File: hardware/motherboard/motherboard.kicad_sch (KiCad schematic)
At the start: 1 part

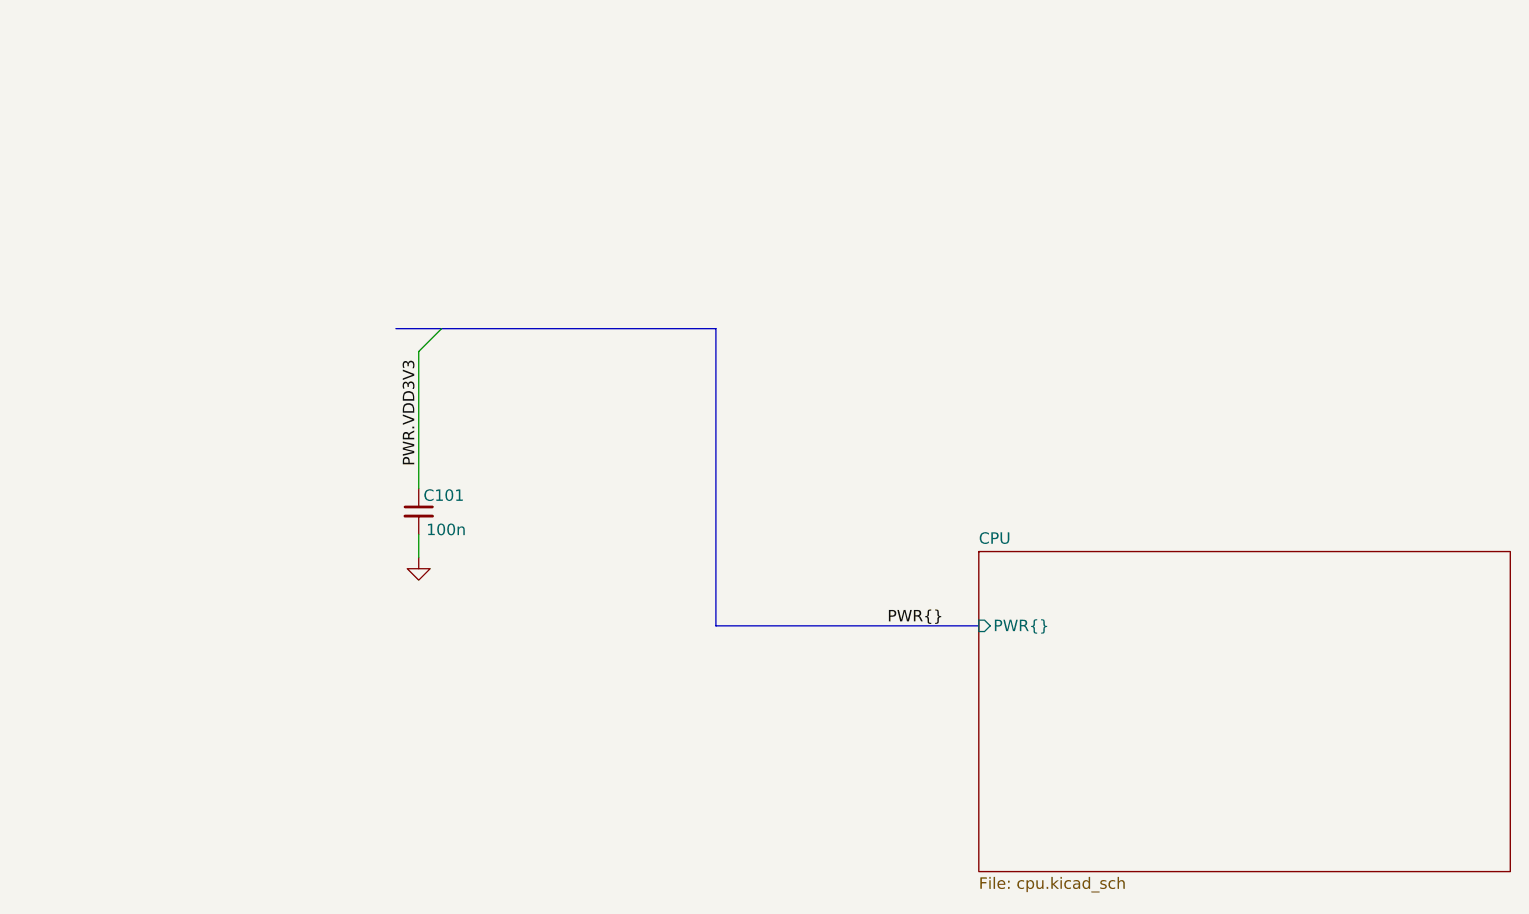
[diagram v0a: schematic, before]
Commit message: Add mp157 family datasheets, fix bus errors in schematic
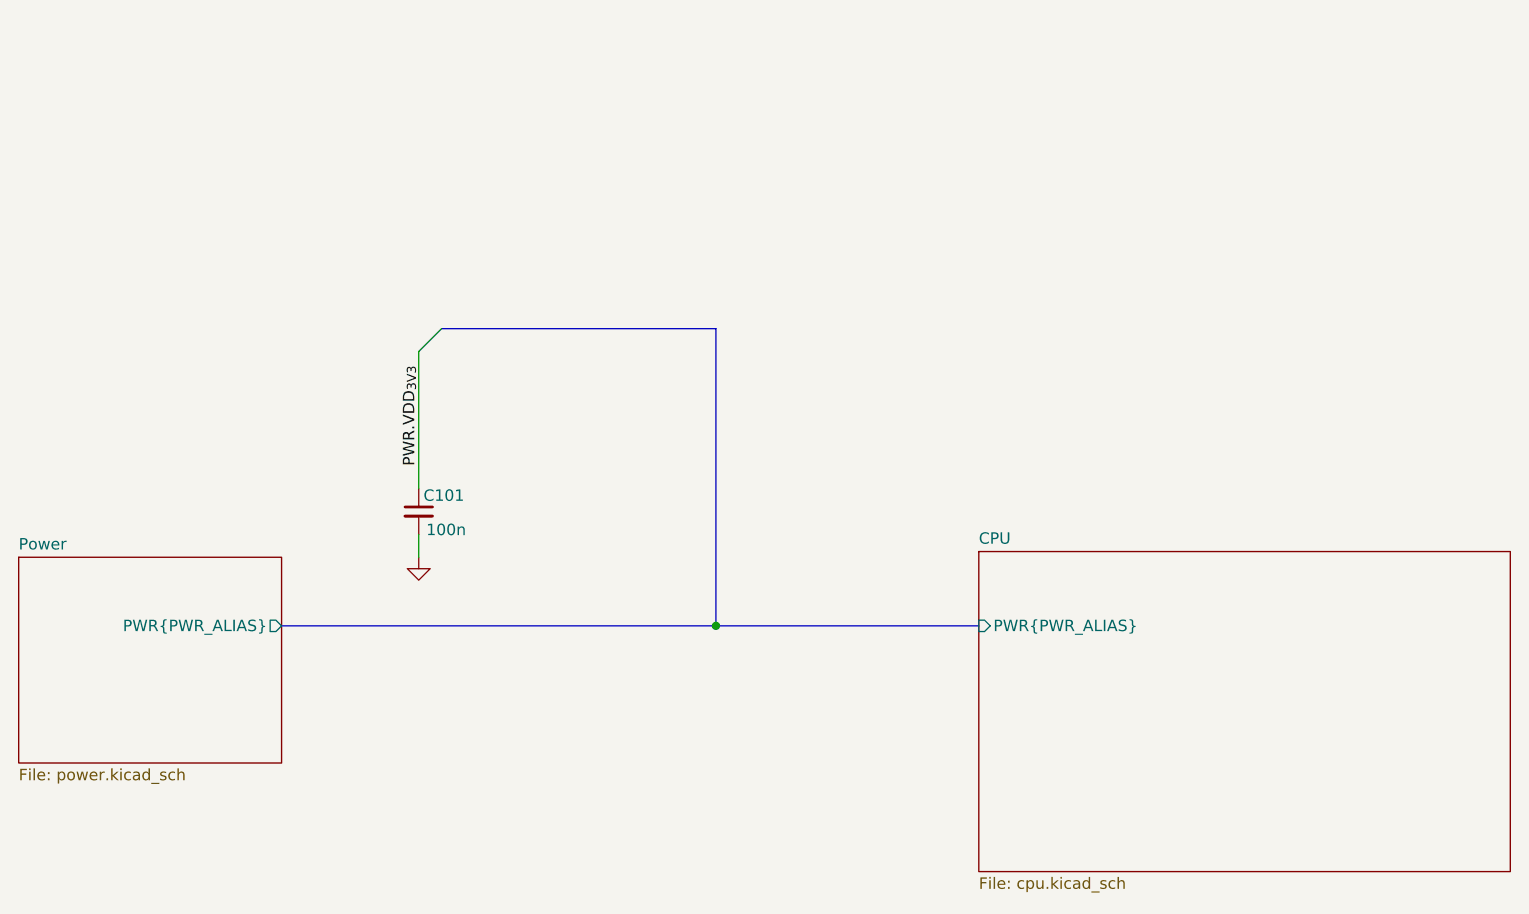
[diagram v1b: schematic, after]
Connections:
- net PWR.VDD3V3 renamed PWR.VDD_{3V3}
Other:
- added sheet Power (power.kicad_sch)
- sheet CPU ports: added PWR{PWR_ALIAS}; removed PWR{}
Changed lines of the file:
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@@
 	(generator_version "8.0")
 	(paper "A3")
+	(junction
+		(at 163.83 208.28)
+		(diameter 0)
+		(color 0 0 0 0)
+	)
 	(bus_entry
 		(at 130.81 177.8)
@@
 	(bus
 		(pts
-			(xy 128.27 175.26) (xy 133.35 175.26)
+			(xy 115.57 208.28) (xy 163.83 208.28)
 		)
 		(stroke
@@
 		)
 	)
-	(label "PWR{}"
-		(at 182.88 208.28 0)
-		(fields_autoplaced yes)
-		(effects
-			(font
-				(size 1.27 1.27)
-			)
-			(justify left bottom)
-		)
-	)
-	(label "PWR.VDD3V3"
+	(label "PWR.VDD_{3V3}"
 		(at 130.81 190.5 90)
 		(fields_autoplaced yes)
@@
 	)
 	(sheet
+		(at 86.36 200.66)
+		(size 29.21 22.86)
+		(fields_autoplaced yes)
+		(stroke
+			(width 0.1524)
+			(type solid)
+		)
+		(fill
+			(color 0 0 0 0.0000)
+		)
+		(property "Sheetname" "Power"
+			(at 86.36 199.9484 0)
+			(effects
+				(font
+					(size 1.27 1.27)
+				)
+				(justify left bottom)
+			)
+		)
+		(property "Sheetfile" "power.kicad_sch"
+			(at 86.36 224.1046 0)
+			(effects
+				(font
+					(size 1.27 1.27)
+				)
+				(justify left top)
+			)
+		)
+		(pin "PWR{PWR_ALIAS}" output
+			(at 115.57 208.28 0)
+			(effects
+				(font
+					(size 1.27 1.27)
+				)
+				(justify right)
+			)
+		)
+		(instances
+			(project "motherboard"
+				(path "/5ade21d8-1dcf-4e66-8082-2cad393a5fdd"
+					(page "3")
+				)
+			)
+		)
+	)
+	(sheet
 		(at 193.04 200.025)
 		(size 59.055 35.56)
@@
 			)
 		)
-		(pin "PWR{}" input
+		(pin "PWR{PWR_ALIAS}" input
 			(at 193.04 208.28 180)
 			(effects
@@
 		)
 		(instances
-			(project "sipzdometr"
+			(project "motherboard"
 				(path "/5ade21d8-1dcf-4e66-8082-2cad393a5fdd"
 					(page "2")

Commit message: Add RAM, models, connect RAM
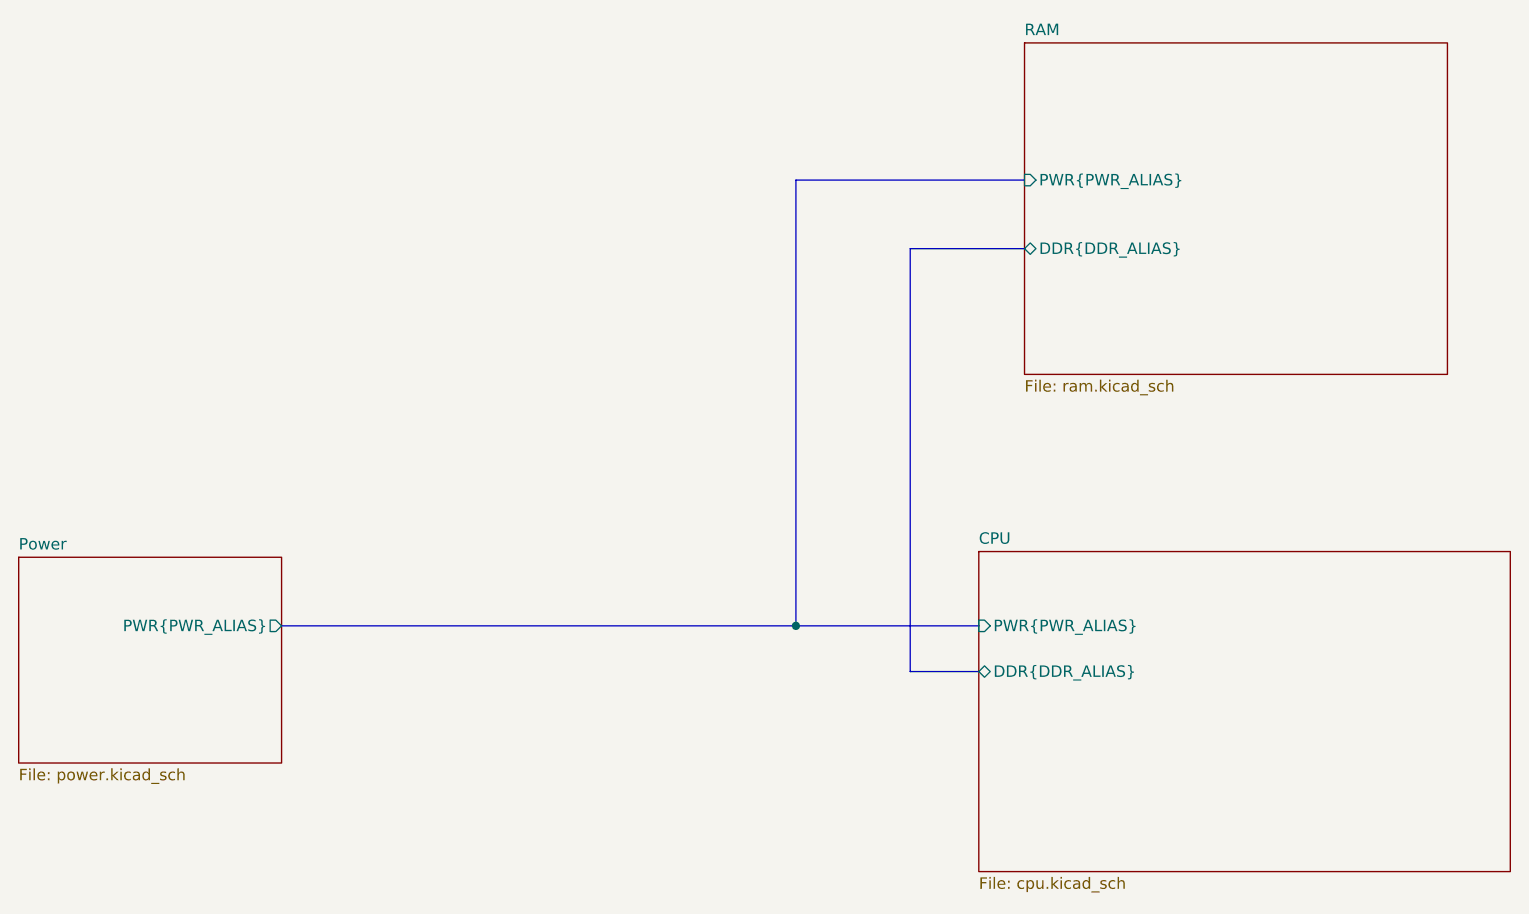
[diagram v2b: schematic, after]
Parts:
- removed C101: 100n, symbol Device:C_Small
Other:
- added sheet RAM (ram.kicad_sch)
- sheet CPU ports: added DDR{DDR_ALIAS}; removed none
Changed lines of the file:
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@@
 	(paper "A3")
 	(junction
-		(at 163.83 208.28)
+		(at 172.72 208.28)
 		(diameter 0)
 		(color 0 0 0 0)
 	)
-	(bus_entry
-		(at 130.81 177.8)
-		(size 2.54 -2.54)
-		(stroke
-			(width 0)
-			(type default)
-		)
-	)
-	(bus
-		(pts
-			(xy 163.83 208.28) (xy 163.83 175.26)
-		)
-		(stroke
-			(width 0)
-			(type default)
-		)
-	)
-	(bus
-		(pts
-			(xy 115.57 208.28) (xy 163.83 208.28)
-		)
-		(stroke
-			(width 0)
-			(type default)
-		)
-	)
-	(bus
-		(pts
-			(xy 193.04 208.28) (xy 163.83 208.28)
-		)
-		(stroke
-			(width 0)
-			(type default)
-		)
-	)
-	(bus
-		(pts
-			(xy 133.35 175.26) (xy 163.83 175.26)
-		)
-		(stroke
-			(width 0)
-			(type default)
-		)
-	)
-	(wire
-		(pts
-			(xy 130.81 198.12) (xy 130.81 200.66)
-		)
-		(stroke
-			(width 0)
-			(type default)
-		)
-	)
-	(wire
-		(pts
-			(xy 130.81 177.8) (xy 130.81 193.04)
-		)
-		(stroke
-			(width 0)
-			(type default)
-		)
-	)
-	(label "PWR.VDD_{3V3}"
-		(at 130.81 190.5 90)
-		(fields_autoplaced yes)
-		(effects
-			(font
-				(size 1.27 1.27)
-			)
-			(justify left bottom)
-		)
-	)
-	(symbol
-		(lib_id "Device:C_Small")
-		(at 130.81 195.58 0)
-		(unit 1)
-		(exclude_from_sim no)
-		(in_bom yes)
-		(on_board yes)
-		(dnp no)
-		(property "Reference" "C101"
-			(at 133.604 193.802 0)
-			(effects
-				(font
-					(size 1.27 1.27)
-				)
-			)
-		)
-		(property "Value" "100n"
-			(at 133.858 197.612 0)
-			(effects
-				(font
-					(size 1.27 1.27)
-				)
-			)
-		)
-		(property "Footprint" ""
-			(at 130.81 195.58 0)
-			(effects
-				(font
-					(size 1.27 1.27)
-				)
-				(hide yes)
-			)
-		)
-		(property "Datasheet" "~"
-			(at 130.81 195.58 0)
-			(effects
-				(font
-					(size 1.27 1.27)
-				)
-				(hide yes)
-			)
-		)
-		(property "Description" "Unpolarized capacitor, small symbol"
-			(at 130.81 195.58 0)
-			(effects
-				(font
-					(size 1.27 1.27)
-				)
-				(hide yes)
-			)
-		)
-		(pin "2"
-		)
-		(pin "1"
-		)
-		(instances
-			(project "sipzdometr"
-				(path "/5ade21d8-1dcf-4e66-8082-2cad393a5fdd"
-					(reference "C101")
-					(unit 1)
-				)
-			)
-		)
-	)
-	(symbol
-		(lib_id "power:GND")
-		(at 130.81 200.66 0)
-		(unit 1)
-		(exclude_from_sim no)
-		(in_bom yes)
-		(on_board yes)
-		(dnp no)
-		(fields_autoplaced yes)
-		(property "Reference" "#PWR0101"
-			(at 130.81 207.01 0)
-			(effects
-				(font
-					(size 1.27 1.27)
-				)
-				(hide yes)
-			)
-		)
-		(property "Value" "GND"
-			(at 130.81 205.74 0)
-			(effects
-				(font
-					(size 1.27 1.27)
-				)
-				(hide yes)
-			)
-		)
-		(property "Footprint" ""
-			(at 130.81 200.66 0)
-			(effects
-				(font
-					(size 1.27 1.27)
-				)
-				(hide yes)
-			)
-		)
-		(property "Datasheet" ""
-			(at 130.81 200.66 0)
-			(effects
-				(font
-					(size 1.27 1.27)
-				)
-				(hide yes)
-			)
-		)
-		(property "Description" "Power symbol creates a global label with name \"GND\" , ground"
-			(at 130.81 200.66 0)
-			(effects
-				(font
-					(size 1.27 1.27)
-				)
-				(hide yes)
-			)
-		)
-		(pin "1"
-		)
-		(instances
-			(project ""
-				(path "/5ade21d8-1dcf-4e66-8082-2cad393a5fdd"
-					(reference "#PWR0101")
-					(unit 1)
-				)
-			)
+	(bus
+		(pts
+			(xy 185.42 166.37) (xy 198.12 166.37)
+		)
+		(stroke
+			(width 0)
+			(type default)
+		)
+	)
+	(bus
+		(pts
+			(xy 172.72 158.75) (xy 172.72 208.28)
+		)
+		(stroke
+			(width 0)
+			(type default)
+		)
+	)
+	(bus
+		(pts
+			(xy 115.57 208.28) (xy 172.72 208.28)
+		)
+		(stroke
+			(width 0)
+			(type default)
+		)
+	)
+	(bus
+		(pts
+			(xy 193.04 208.28) (xy 172.72 208.28)
+		)
+		(stroke
+			(width 0)
+			(type default)
+		)
+	)
+	(bus
+		(pts
+			(xy 185.42 213.36) (xy 185.42 166.37)
+		)
+		(stroke
+			(width 0)
+			(type default)
+		)
+	)
+	(bus
+		(pts
+			(xy 193.04 213.36) (xy 185.42 213.36)
+		)
+		(stroke
+			(width 0)
+			(type default)
+		)
+	)
+	(bus
+		(pts
+			(xy 198.12 158.75) (xy 172.72 158.75)
+		)
+		(stroke
+			(width 0)
+			(type default)
 		)
 	)
@@
 			)
 		)
+		(pin "DDR{DDR_ALIAS}" bidirectional
+			(at 193.04 213.36 180)
+			(effects
+				(font
+					(size 1.27 1.27)
+				)
+				(justify left)
+			)
+		)
 		(instances
 			(project "motherboard"
@@
 				)
 			)
+		)
+	)
+	(sheet
+		(at 198.12 143.51)
+		(size 46.99 36.83)
+		(fields_autoplaced yes)
+		(stroke
+			(width 0.1524)
+			(type solid)
+		)
+		(fill
+			(color 0 0 0 0.0000)
+		)
+		(property "Sheetname" "RAM"
+			(at 198.12 142.7984 0)
+			(effects
+				(font
+					(size 1.27 1.27)
+				)
+				(justify left bottom)
+			)
+		)
+		(property "Sheetfile" "ram.kicad_sch"
+			(at 198.12 180.9246 0)
+			(effects
+				(font
+					(size 1.27 1.27)
+				)
+				(justify left top)
+			)
+		)
+		(pin "DDR{DDR_ALIAS}" bidirectional
+			(at 198.12 166.37 180)
+			(effects
+				(font
+					(size 1.27 1.27)
+				)
+				(justify left)
+			)
+		)
+		(pin "PWR{PWR_ALIAS}" input
+			(at 198.12 158.75 180)
+			(effects
+				(font
+					(size 1.27 1.27)
+				)
+				(justify left)
+			)
+		)
+		(instances
+			(project "motherboard"
+				(path "/5ade21d8-1dcf-4e66-8082-2cad393a5fdd"
+					(page "4")
+				)
+			)
